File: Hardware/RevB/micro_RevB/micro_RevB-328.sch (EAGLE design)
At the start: 39 parts, among them Q101 CSTCR6M00G53Z, U101 ATMEGA328P, U102 TLC59711, U103 LP2985AIM5-3.3

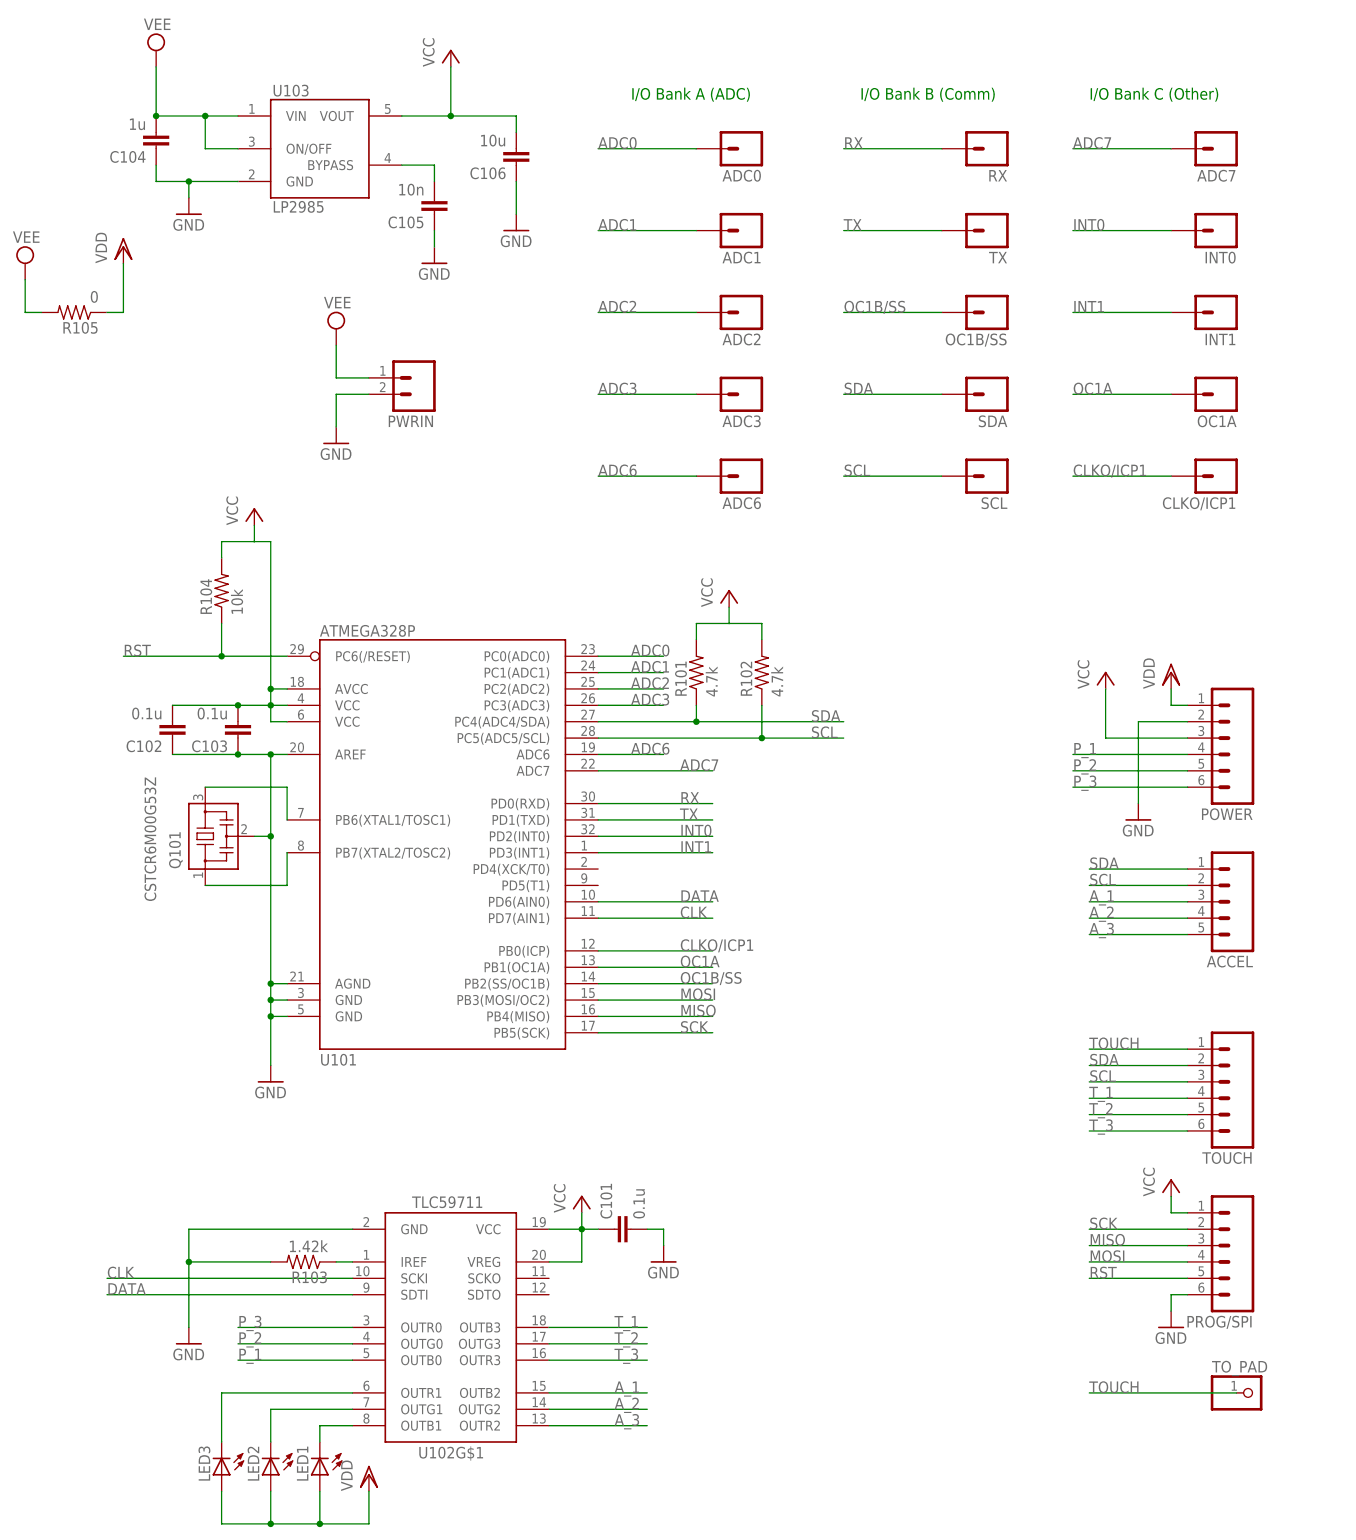
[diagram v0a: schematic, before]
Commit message: Routing micro RevB
micro RevB is about half routed; schematic had a few errors corrected;
added a notes file to keep track of the things to be kept standard.
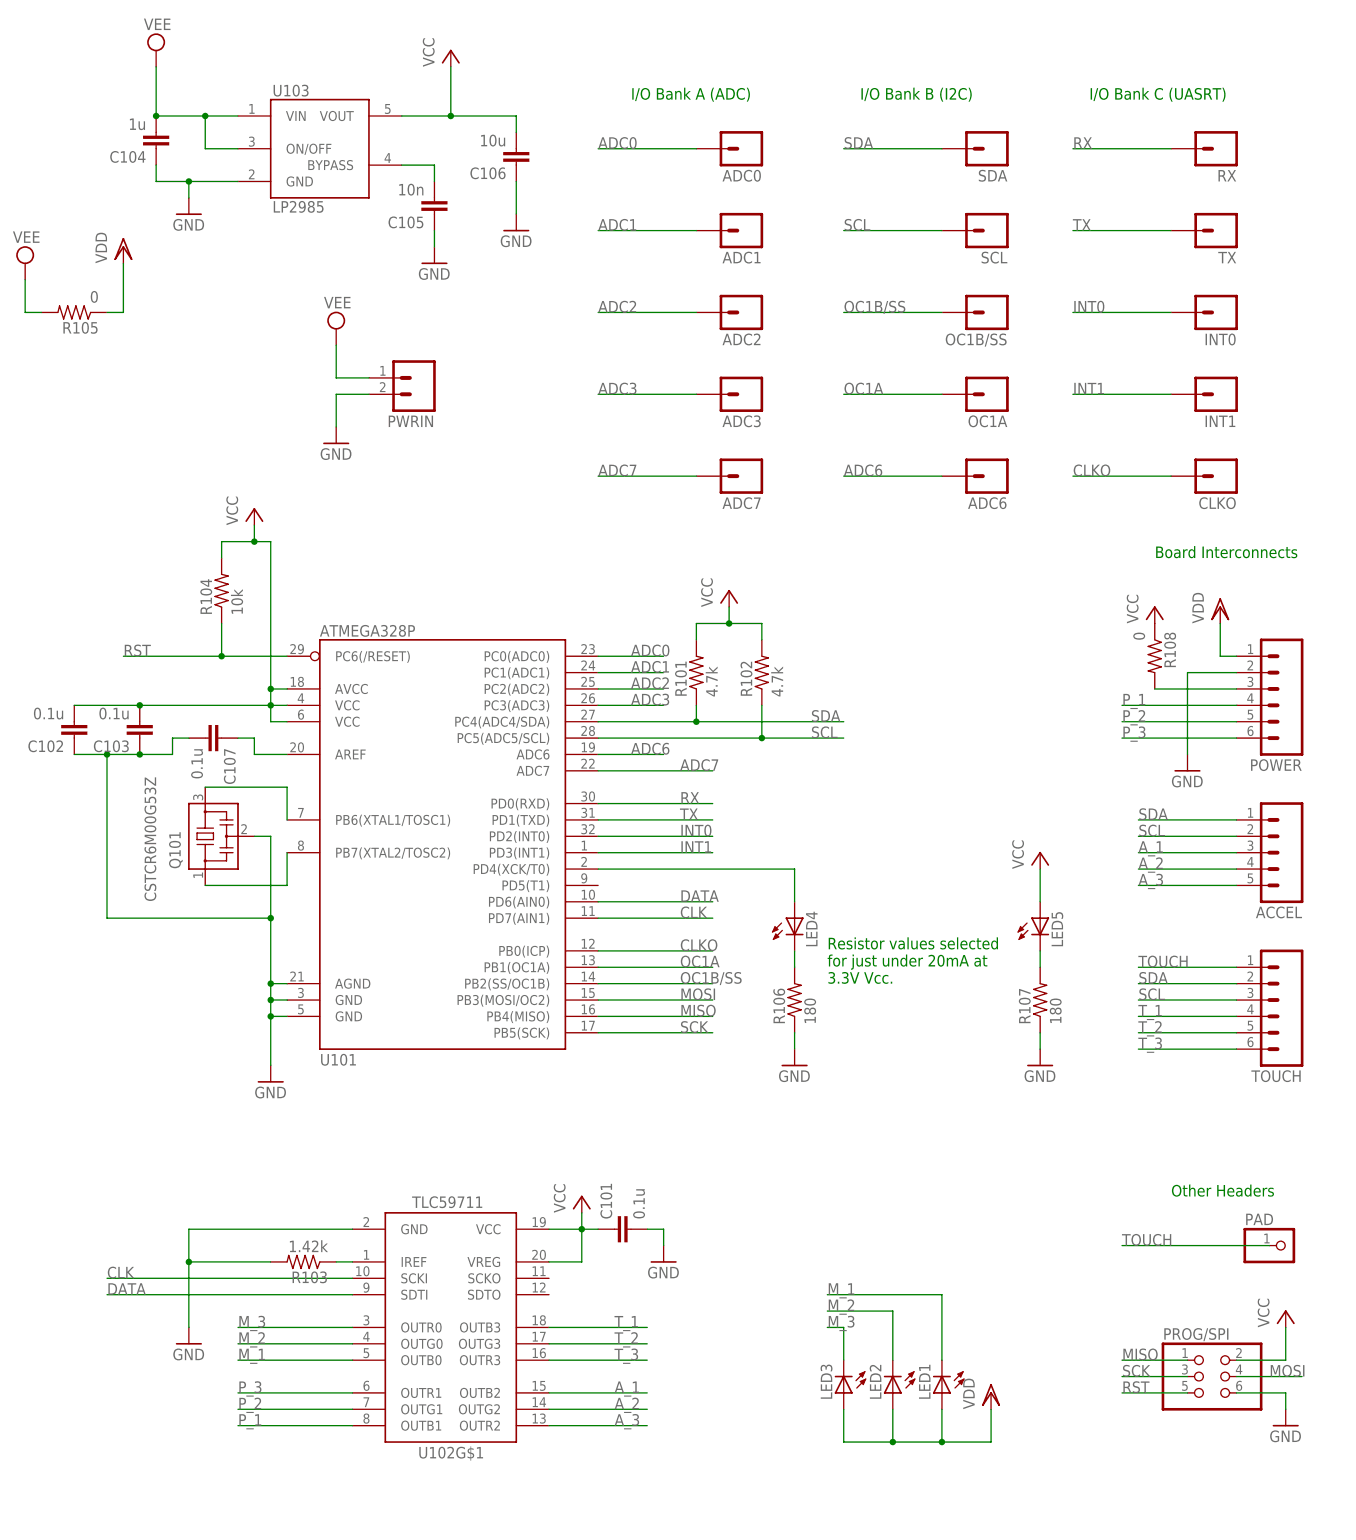
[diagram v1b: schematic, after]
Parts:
- removed TO_PAD: (no value), pinhead:PINHD-1X1
- added C107: 0.1u, eagle-ltspice:CC0603
- added LED4, LED5: (no value), led:LEDSML0603
- added PAD: (no value), pinhead:PINHD-1X1
- added R106, R107: 180, rcl:R-US_R0603
- added R108: 0, rcl:R-US_R0603
- PROG/SPI: device SparkFun-Connectors:M06SIP_LOCK -> SparkFun-Connectors:PINHD-2X3
- renumbered CLKO/ICP1 to CLKO
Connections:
- removed net CLKO/ICP1: U101.PB0(ICP)
- removed net N$6: LED2.C, U102G$1.OUTG1
- removed net N$7: LED1.C, U102G$1.OUTB1
- new net CLKO: CLKO.1, U101.PB0(ICP)
- new net M_1: LED1.C, U102G$1.OUTB0
- new net M_2: LED2.C, U102G$1.OUTG0
- new net M_3: LED3.C, U102G$1.OUTR0
- new net N$10: C107.1, U101.AREF
- new net N$12: LED5.C, R107.2
- new net N$3: LED4.A, U101.PD4(XCK/T0)
- new net N$8: LED4.C, R106.2
- net GND: now also C107.2, R106.1, R107.1; no longer U101.AREF
- net MISO: now also PROG/SPI.1; no longer PROG/SPI.3
- net N$5: now also POWER.3, R108.2; no longer LED3.C, U102G$1.OUTR1
- net P_1: now also U102G$1.OUTB1; no longer U102G$1.OUTB0
- net P_2: now also U102G$1.OUTG1; no longer U102G$1.OUTG0
- net P_3: now also U102G$1.OUTR1; no longer U102G$1.OUTR0
- net SCK: now also PROG/SPI.3; no longer PROG/SPI.2
- net SDA: now also SDA.1
- net TOUCH: now also PAD.1; no longer TO_PAD.1
- net VCC: now also LED5.A, PROG/SPI.2, R108.1; no longer POWER.3, PROG/SPI.1
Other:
- note added: "Board Interconnects"
- note added: "I/O Bank B (I2C)"
- note added: "I/O Bank C (UASRT)"
- note added: "Other Headers"
- note added: "Resistor values selected for just under 20mA at 3.3V Vcc."
- note removed: "I/O Bank B (Comm)"
- note removed: "I/O Bank C (Other)"
- moved on the sheet: ACCEL, ADC6, ADC7, C102, C103, INT0, INT1, LED1, LED2, LED3, OC1A, POWER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

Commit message: Progress on routing micron RevB
Done routing; working on the silkcreening; probably changing the ADC
individual pins to a 5 pin header.
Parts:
- removed RX, SCL, SDA, TX: M01PTH, SparkFun-Connectors:M01PTH
- added I2C, PWROUT, UART: M02LOCK, SparkFun-Connectors:M02LOCK
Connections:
- removed net GND: C101.2, C102.1, C103.1, C104.1, C105.1, C106.1, C107.2, POWER.2, PROG/SPI.6, PWRIN.2, Q101.2, R103.2, R106.1, R107.1, U101.AGND, U101.GND@1, U101.GND@2, U102G$1.GND, U103.GND
- new net N7: C101.2, C102.1, C103.1, C104.1, C105.1, C106.1, C107.2, POWER.2, PROG/SPI.6, PWRIN.2, PWROUT.2, Q101.2, R103.2, R106.1, R107.1, U101.AGND, U101.GND@1, U101.GND@2, U102G$1.GND, U103.GND
- net RX: now also UART.1; no longer RX.1
- net SCL: now also I2C.2; no longer SCL.1
- net SDA: now also I2C.1; no longer SDA.1
- net TX: now also UART.2; no longer TX.1
- net VCC: now also PWROUT.1
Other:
- moved on the sheet: ADC6, CLKO, INT0, INT1, OC1A, OC1B/SS, PWRIN
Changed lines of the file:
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@@
 <part name="ADC3" library="SparkFun-Connectors" deviceset="M01" device="PTH" value=""/>
 <part name="ADC6" library="SparkFun-Connectors" deviceset="M01" device="PTH" value=""/>
-<part name="RX" library="SparkFun-Connectors" deviceset="M01" device="PTH" value=""/>
-<part name="TX" library="SparkFun-Connectors" deviceset="M01" device="PTH" value=""/>
 <part name="OC1B/SS" library="SparkFun-Connectors" deviceset="M01" device="PTH" value=""/>
-<part name="SDA" library="SparkFun-Connectors" deviceset="M01" device="PTH" value=""/>
-<part name="SCL" library="SparkFun-Connectors" deviceset="M01" device="PTH" value=""/>
 <part name="ADC7" library="SparkFun-Connectors" deviceset="M01" device="PTH" value=""/>
 <part name="INT0" library="SparkFun-Connectors" deviceset="M01" device="PTH" value=""/>
@@
 <part name="PROG/SPI" library="SparkFun-Connectors" deviceset="PINHD-2X3" device=""/>
 <part name="R108" library="rcl" deviceset="R-US_" device="R0603" value="0"/>
+<part name="PWROUT" library="SparkFun-Connectors" deviceset="M02" device="LOCK" value=""/>
+<part name="P+8" library="supply1" deviceset="VCC" device=""/>
+<part name="GND12" library="supply1" deviceset="GND" device=""/>
+<part name="UART" library="SparkFun-Connectors" deviceset="M02" device="LOCK" value=""/>
+<part name="I2C" library="SparkFun-Connectors" deviceset="M02" device="LOCK" value=""/>
 </parts>
 <sheets>
@@
 <instance part="ADC2" gate="G$1" x="127" y="134.62" rot="R180"/>
 <instance part="ADC3" gate="G$1" x="127" y="121.92" rot="R180"/>
-<instance part="ADC6" gate="G$1" x="165.1" y="109.22" rot="R180"/>
-<instance part="RX" gate="G$1" x="200.66" y="160.02" rot="R180"/>
-<instance part="TX" gate="G$1" x="200.66" y="147.32" rot="R180"/>
-<instance part="OC1B/SS" gate="G$1" x="165.1" y="134.62" rot="R180"/>
-<instance part="SDA" gate="G$1" x="165.1" y="160.02" rot="R180"/>
-<instance part="SCL" gate="G$1" x="165.1" y="147.32" rot="R180"/>
+<instance part="ADC6" gate="G$1" x="165.1" y="119.38" rot="R180"/>
+<instance part="OC1B/SS" gate="G$1" x="165.1" y="144.78" rot="R180"/>
 <instance part="ADC7" gate="G$1" x="127" y="109.22" rot="R180"/>
-<instance part="INT0" gate="G$1" x="200.66" y="134.62" rot="R180"/>
-<instance part="INT1" gate="G$1" x="200.66" y="121.92" rot="R180"/>
-<instance part="OC1A" gate="G$1" x="165.1" y="121.92" rot="R180"/>
-<instance part="CLKO" gate="G$1" x="200.66" y="109.22" rot="R180"/>
-<instance part="PWRIN" gate="G$1" x="76.2" y="124.46" rot="R180"/>
-<instance part="GND9" gate="1" x="63.5" y="114.3"/>
-<instance part="SUPPLY3" gate="G$1" x="63.5" y="132.08"/>
+<instance part="INT0" gate="G$1" x="200.66" y="144.78" rot="R180"/>
+<instance part="INT1" gate="G$1" x="200.66" y="132.08" rot="R180"/>
+<instance part="OC1A" gate="G$1" x="165.1" y="132.08" rot="R180"/>
+<instance part="CLKO" gate="G$1" x="200.66" y="119.38" rot="R180"/>
+<instance part="PWRIN" gate="G$1" x="58.42" y="124.46" rot="R180"/>
+<instance part="GND9" gate="1" x="45.72" y="114.3"/>
+<instance part="SUPPLY3" gate="G$1" x="45.72" y="132.08"/>
 <instance part="POWER" gate="G$1" x="208.28" y="76.2" rot="R180"/>
 <instance part="TOUCH" gate="G$1" x="208.28" y="27.94" rot="R180"/>
@@
 <instance part="PROG/SPI" gate="A" x="198.12" y="-30.48"/>
 <instance part="R108" gate="G$1" x="190.5" y="81.28" rot="R270"/>
+<instance part="PWROUT" gate="G$1" x="83.82" y="124.46" rot="R180"/>
+<instance part="P+8" gate="VCC" x="71.12" y="134.62"/>
+<instance part="GND12" gate="1" x="71.12" y="114.3"/>
+<instance part="UART" gate="G$1" x="200.66" y="160.02" rot="R180"/>
+<instance part="I2C" gate="G$1" x="165.1" y="160.02" rot="R180"/>
 </instances>
 <busses>
@@
 <pinref part="P+4" gate="VCC" pin="VCC"/>
 </segment>
-</net>
-<net name="GND" class="0">
+<segment>
+<pinref part="P+8" gate="VCC" pin="VCC"/>
+<pinref part="PWROUT" gate="G$1" pin="1"/>
+<wire x1="71.12" y1="132.08" x2="71.12" y2="124.46" width="0.1524" layer="91"/>
+<wire x1="71.12" y1="124.46" x2="76.2" y2="124.46" width="0.1524" layer="91"/>
+</segment>
+</net>
+<net name="N7" class="0">
 <segment>
 <pinref part="U101" gate="G$1" pin="AGND"/>
@@
 <segment>
 <pinref part="PWRIN" gate="G$1" pin="2"/>
-<wire x1="68.58" y1="121.92" x2="63.5" y2="121.92" width="0.1524" layer="91"/>
-<wire x1="63.5" y1="121.92" x2="63.5" y2="116.84" width="0.1524" layer="91"/>
+<wire x1="50.8" y1="121.92" x2="45.72" y2="121.92" width="0.1524" layer="91"/>
+<wire x1="45.72" y1="121.92" x2="45.72" y2="116.84" width="0.1524" layer="91"/>
 <pinref part="GND9" gate="1" pin="GND"/>
 </segment>
@@
 <pinref part="R107" gate="G$1" pin="1"/>
 <wire x1="172.72" y1="20.32" x2="172.72" y2="22.86" width="0.1524" layer="91"/>
+</segment>
+<segment>
+<pinref part="PWROUT" gate="G$1" pin="2"/>
+<pinref part="GND12" gate="1" pin="GND"/>
+<wire x1="76.2" y1="121.92" x2="71.12" y2="121.92" width="0.1524" layer="91"/>
+<wire x1="71.12" y1="121.92" x2="71.12" y2="116.84" width="0.1524" layer="91"/>
 </segment>
 </net>
@@
 <wire x1="157.48" y1="160.02" x2="142.24" y2="160.02" width="0.1524" layer="91"/>
 <label x="142.24" y="160.02" size="1.778" layer="95"/>
-<pinref part="SDA" gate="G$1" pin="1"/>
+<pinref part="I2C" gate="G$1" pin="1"/>
 </segment>
 </net>
@@
 </segment>
 <segment>
-<pinref part="SCL" gate="G$1" pin="1"/>
-<wire x1="157.48" y1="147.32" x2="142.24" y2="147.32" width="0.1524" layer="91"/>
-<label x="142.24" y="147.32" size="1.778" layer="95"/>
+<pinref part="I2C" gate="G$1" pin="2"/>
+<wire x1="157.48" y1="157.48" x2="142.24" y2="157.48" width="0.1524" layer="91"/>
+<label x="142.24" y="157.48" size="1.778" layer="95"/>
 </segment>
 </net>
@@
 <segment>
 <pinref part="PWRIN" gate="G$1" pin="1"/>
-<wire x1="68.58" y1="124.46" x2="63.5" y2="124.46" width="0.1524" layer="91"/>
-<wire x1="63.5" y1="124.46" x2="63.5" y2="129.54" width="0.1524" layer="91"/>
+<wire x1="50.8" y1="124.46" x2="45.72" y2="124.46" width="0.1524" layer="91"/>
+<wire x1="45.72" y1="124.46" x2="45.72" y2="129.54" width="0.1524" layer="91"/>
 <pinref part="SUPPLY3" gate="G$1" pin="VEE"/>
 </segment>
@@
 <segment>
 <pinref part="ADC6" gate="G$1" pin="1"/>
-<wire x1="157.48" y1="109.22" x2="142.24" y2="109.22" width="0.1524" layer="91"/>
-<label x="142.24" y="109.22" size="1.778" layer="95"/>
+<wire x1="157.48" y1="119.38" x2="142.24" y2="119.38" width="0.1524" layer="91"/>
+<label x="142.24" y="119.38" size="1.778" layer="95"/>
 </segment>
 <segment>
@@
 </segment>
 <segment>
-<pinref part="RX" gate="G$1" pin="1"/>
+<pinref part="UART" gate="G$1" pin="1"/>
 <wire x1="193.04" y1="160.02" x2="177.8" y2="160.02" width="0.1524" layer="91"/>
 <label x="177.8" y="160.02" size="1.778" layer="95"/>
@@
 </segment>
 <segment>
-<pinref part="TX" gate="G$1" pin="1"/>
-<wire x1="193.04" y1="147.32" x2="177.8" y2="147.32" width="0.1524" layer="91"/>
-<label x="177.8" y="147.32" size="1.778" layer="95"/>
+<pinref part="UART" gate="G$1" pin="2"/>
+<wire x1="193.04" y1="157.48" x2="177.8" y2="157.48" width="0.1524" layer="91"/>
+<label x="177.8" y="157.48" size="1.778" layer="95"/>
 </segment>
 </net>
@@
 <segment>
 <pinref part="INT0" gate="G$1" pin="1"/>
-<wire x1="193.04" y1="134.62" x2="177.8" y2="134.62" width="0.1524" layer="91"/>
-<label x="177.8" y="134.62" size="1.778" layer="95"/>
+<wire x1="193.04" y1="144.78" x2="177.8" y2="144.78" width="0.1524" layer="91"/>
+<label x="177.8" y="144.78" size="1.778" layer="95"/>
 </segment>
 </net>
@@
 <segment>
 <pinref part="INT1" gate="G$1" pin="1"/>
-<wire x1="193.04" y1="121.92" x2="177.8" y2="121.92" width="0.1524" layer="91"/>
-<label x="177.8" y="121.92" size="1.778" layer="95"/>
+<wire x1="193.04" y1="132.08" x2="177.8" y2="132.08" width="0.1524" layer="91"/>
+<label x="177.8" y="132.08" size="1.778" layer="95"/>
 </segment>
 </net>
@@
 <segment>
 <pinref part="OC1A" gate="G$1" pin="1"/>
-<wire x1="157.48" y1="121.92" x2="142.24" y2="121.92" width="0.1524" layer="91"/>
-<label x="142.24" y="121.92" size="1.778" layer="95"/>
+<wire x1="157.48" y1="132.08" x2="142.24" y2="132.08" width="0.1524" layer="91"/>
+<label x="142.24" y="132.08" size="1.778" layer="95"/>
 </segment>
 </net>
@@
 <segment>
 <pinref part="OC1B/SS" gate="G$1" pin="1"/>
-<wire x1="157.48" y1="134.62" x2="142.24" y2="134.62" width="0.1524" layer="91"/>
-<label x="142.24" y="134.62" size="1.778" layer="95"/>
+<wire x1="157.48" y1="144.78" x2="142.24" y2="144.78" width="0.1524" layer="91"/>
+<label x="142.24" y="144.78" size="1.778" layer="95"/>
 </segment>
 </net>
@@
 </segment>
 <segment>
-<wire x1="193.04" y1="109.22" x2="177.8" y2="109.22" width="0.1524" layer="91"/>
-<label x="177.8" y="109.22" size="1.778" layer="95"/>
+<wire x1="193.04" y1="119.38" x2="177.8" y2="119.38" width="0.1524" layer="91"/>
+<label x="177.8" y="119.38" size="1.778" layer="95"/>
 <pinref part="CLKO" gate="G$1" pin="1"/>
 </segment>
